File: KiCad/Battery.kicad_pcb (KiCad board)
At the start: 2 copper layers, 19 x 29 mm, 22 parts, among them J1 Connector, J2 USB-C, J3 DC, Q1 RN1701, Q2 BSS169, U1 ESP32-WROOM-32, U2 FT231XQ

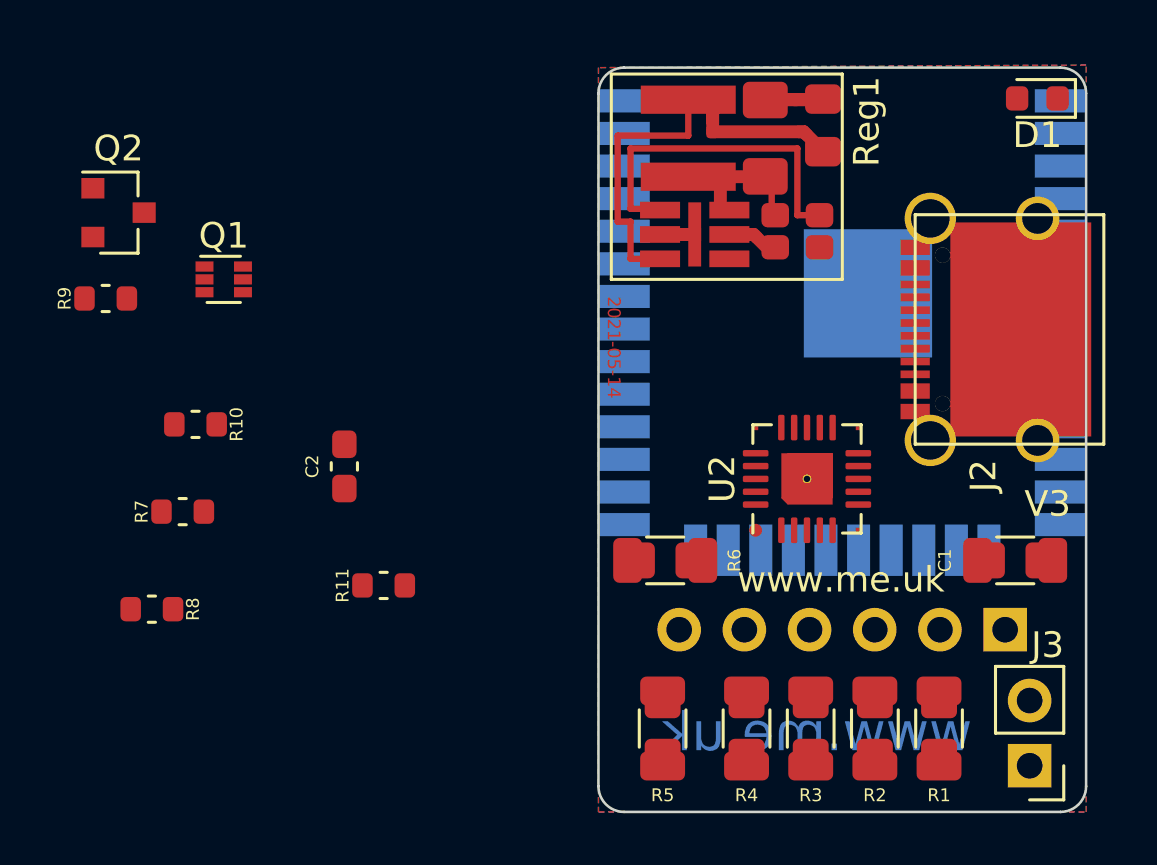
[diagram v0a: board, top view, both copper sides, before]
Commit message: New battery based module (i.e. usb can be totally powered down)
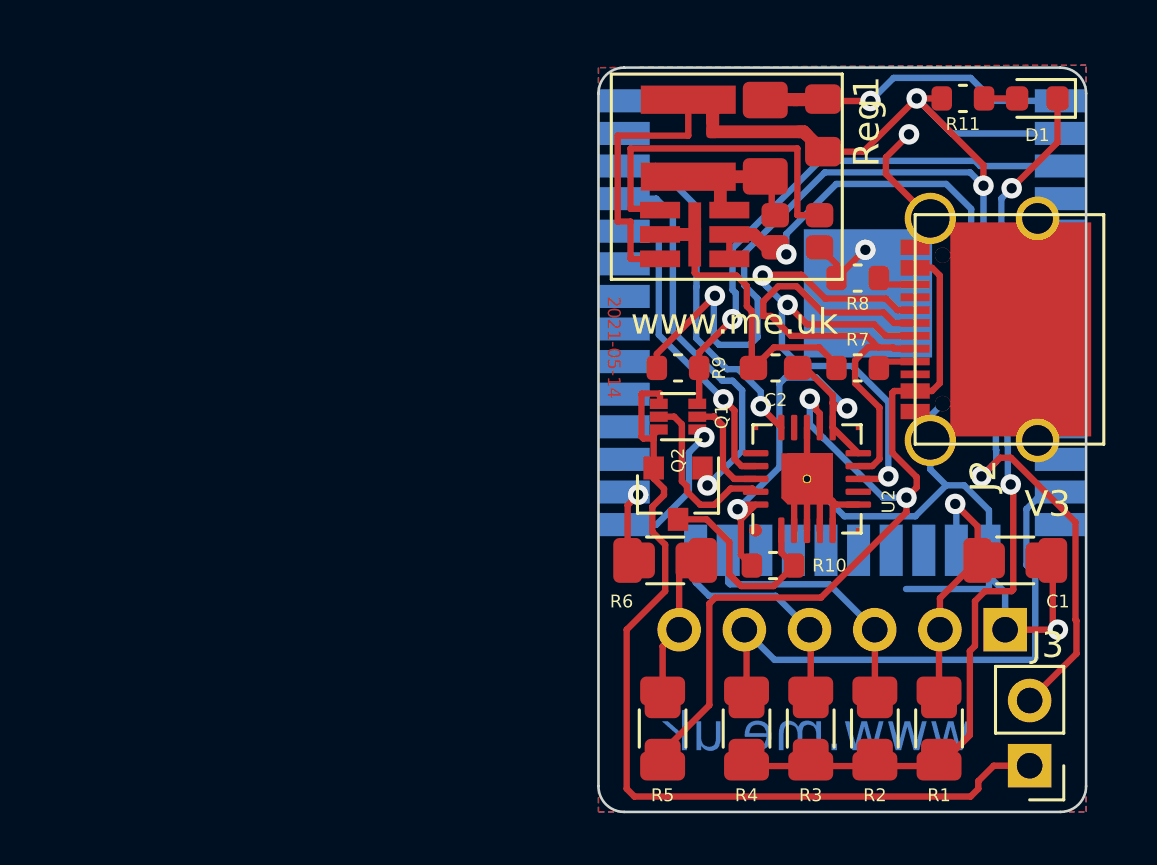
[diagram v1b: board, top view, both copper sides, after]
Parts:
- moved R8 30.4 mm to (127.3, 106.8), turned to 0 degrees
- moved R11 29.5 mm to (131.4, 99.8)
- moved R7 26.9 mm to (127.3, 110.3), turned to 180 degrees
- moved Q2 24.4 mm to (120.3, 115.2), turned to 270 degrees
- moved R10 23.2 mm to (124.0, 118.0), turned to 0 degrees
- moved R9 22.5 mm to (120.3, 110.3), turned to 180 degrees
- moved Q1 18.5 mm to (120.3, 112.2), turned to 180 degrees
- moved C2 17.2 mm to (124.1, 110.3), turned to 180 degrees
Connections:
- Q1 pad 1: Net-(D1-Pad1) -> Net-(Q1-Pad1)
- U1 pad 10: Net-(U1-Pad10) -> Net-(D1-Pad1)
- U1 pad 25: Net-(D1-Pad1) -> Net-(Q1-Pad1)
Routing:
- net GND: track 0.00 -> 111.7 mm, vias 0 -> 4
- net +3V3: track 0.00 -> 70.2 mm, vias 0 -> 4
- net VBUS: track 0.00 -> 35.4 mm, vias 0 -> 2
- net Net-(J3-Pad2): track 0.00 -> 34.5 mm, vias 0 -> 2
- net D+: track 0.00 -> 24.5 mm, vias 0 -> 3
- net IO4: track 0.00 -> 21.8 mm
- net Net-(Q1-Pad3): track 0.00 -> 21.0 mm, vias 0 -> 1
- net D-: track 0.00 -> 20.1 mm
- net USB3.3: track 0.00 -> 17.2 mm, vias 0 -> 2
- net Net-(Q2-Pad1): track 0.00 -> 15.4 mm, vias 0 -> 1
- net Net-(D1-Pad1): track 0.00 -> 14.3 mm, vias 0 -> 1
- net CBUS: track 0.00 -> 13.7 mm, vias 0 -> 1
- net I: track 0.00 -> 12.3 mm, vias 0 -> 1
- net IO2: track 0.00 -> 10.1 mm
- net IO1: track 0.00 -> 10.1 mm, vias 0 -> 1
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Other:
- net class Close added: clearance 0.1, trace_width 0.25, via_dia 0.8, via_drill 0.4

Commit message: Regulator update
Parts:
- moved R8 0.20 mm to (127.5, 106.8)
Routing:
- net GND: track 111.7 -> 135.7 mm, vias 4 -> 5
- net D+: track 24.5 -> 23.8 mm
- net Net-(J3-Pad2): track 34.5 -> 35.0 mm, vias 2 -> 3

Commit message: Tweak
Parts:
- moved Reg1 0.46 mm to (120.5, 105.0)
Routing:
- net GND: track 135.7 -> 128.0 mm
- net Net-(J3-Pad2): track 35.0 -> 34.6 mm, vias 3 -> 2

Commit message: 18K
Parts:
- added Q3: BSS169, Package_TO_SOT_SMD:SOT-23, F.Cu at (128.1, 101.5)
- added R12: 18K, RevK:R_0603, F.Cu at (127.5, 103.8)
- added R13: 1k, RevK:R_0603, F.Cu at (130.4, 102.0)
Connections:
- net Net-(J3-Pad2) renamed DC
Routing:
- net Net-(R12-Pad2): track 0.00 -> 20.0 mm, vias 0 -> 1
- net GND: track 128.0 -> 147.2 mm, vias 5 -> 4
- net Net-(Q3-Pad1): track 0.00 -> 16.9 mm, vias 0 -> 1
- net VBUS: track 35.9 -> 51.0 mm
- net DC: track 34.6 -> 40.7 mm, vias 2 -> 3
- net Net-(Q1-Pad3): track 20.9 -> 24.9 mm
- net USB3.3: track 17.3 -> 15.3 mm
- net D+: track 23.8 -> 25.8 mm
- net D-: track 19.6 -> 21.5 mm
- net +3V3: track 69.6 -> 71.3 mm
- net Net-(Q3-Pad2): track 0.00 -> 1.53 mm
- net Net-(D1-Pad1): track 14.7 -> 15.6 mm
- net CBUS: track 13.7 -> 14.5 mm
- net Net-(Q2-Pad1): track 15.3 -> 15.9 mm
